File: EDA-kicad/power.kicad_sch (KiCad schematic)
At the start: 97 parts, among them SW1 EG25-switch-CSS-1210MC, SW2 MIC-switch-CSS-1210MC, SW3 CAM-switch-CSS-1210MC, U11 TPS65023BRSBR, U4 BQ25792RQMR, U6 BAT-CONNECTOR-FLTS22WR00, U7 22V-boost-AP3032KTR-G1, U8 MP3429GL-Z

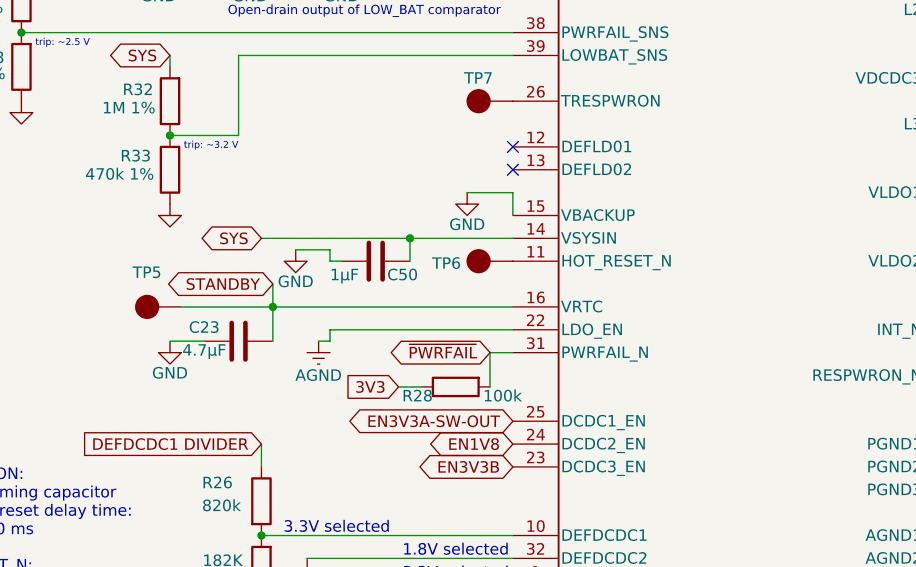
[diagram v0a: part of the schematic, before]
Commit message: applied no backup bat config to VSYSIN, removed standby label
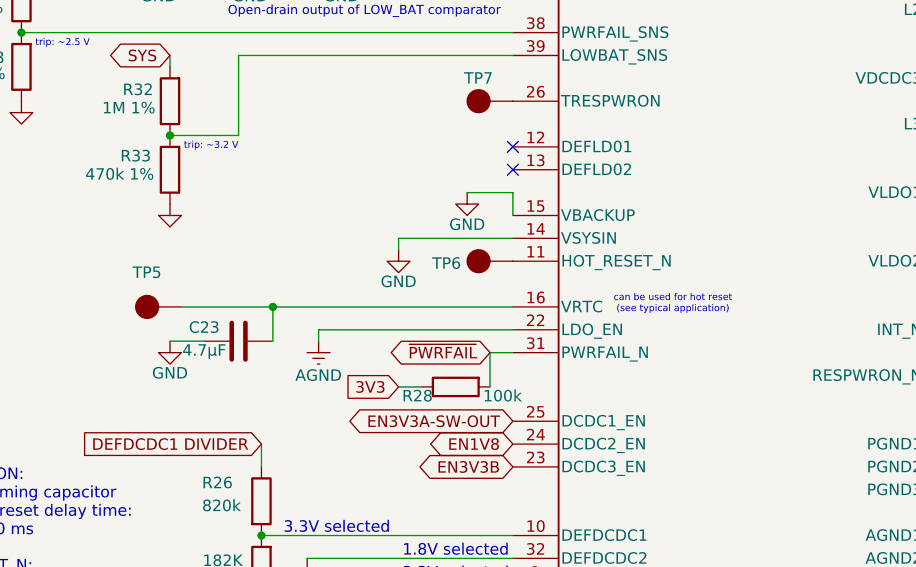
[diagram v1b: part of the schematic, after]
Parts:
- removed C50: 1μF, SPIRIT-footprints:0603-capacitor, symbol Device:C
- added C23: 4.7μF, SPIRIT-footprints:0603-capacitor, symbol Device:C
- added R33: 470k 1%, SPIRIT-footprints:0603-resistor, symbol Device:R
- renumbered C23 to C10, R33 to R8
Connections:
- net GND: now also U11.14 (VSYSIN), C23.1, R33.1; no longer C10.1
- net SYS: no longer U11.14 (VSYSIN)
- net at R32.1, U11.39 (LOWBAT_SNS): now also R33.2; no longer R8.2
- net STANDBY: no longer names the net of TP5.1 (A), U11.16 (VRTC)
- net STANDBY: now also C23.2; no longer C10.2
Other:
- note added: "can be used for hot reset (see typical application)"
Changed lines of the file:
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@@
 		)
 	)
+	(text "can be used for hot reset\n(see typical application)"
+		(exclude_from_sim no)
+		(at 321.31 135.636 0)
+		(effects
+			(font
+				(size 0.762 0.762)
+			)
+		)
+	)
 	(text "40mA selected for backlight LED"
 		(exclude_from_sim no)
@@
 	)
 	(junction
-		(at 292.1 128.27)
-		(diameter 0)
-		(color 0 0 0 0)
-	)
-	(junction
 		(at 146.05 238.76)
 		(diameter 0)
@@
 	(wire
 		(pts
-			(xy 283.21 130.81) (xy 284.48 130.81)
-		)
-		(stroke
-			(width 0)
-			(type default)
-		)
-	)
-	(wire
-		(pts
 			(xy 306.07 226.06) (xy 302.26 226.06)
 		)
@@
 	(wire
 		(pts
-			(xy 275.59 128.27) (xy 292.1 128.27)
-		)
-		(stroke
-			(width 0)
-			(type default)
-		)
-	)
-	(wire
-		(pts
 			(xy 298.45 81.28) (xy 298.45 88.9)
 		)
@@
 	(wire
 		(pts
-			(xy 283.21 138.43) (xy 303.53 138.43)
-		)
-		(stroke
-			(width 0)
-			(type default)
-		)
-	)
-	(wire
-		(pts
 			(xy 62.23 194.31) (xy 62.23 190.5)
 		)
@@
 	(wire
 		(pts
-			(xy 276.86 133.35) (xy 276.86 135.89)
-		)
-		(stroke
-			(width 0)
-			(type default)
-		)
-	)
-	(wire
-		(pts
 			(xy 369.57 119.38) (xy 372.11 119.38)
 		)
@@
 	(wire
 		(pts
-			(xy 372.11 93.98) (xy 369.57 93.98)
+			(xy 281.94 138.43) (xy 303.53 138.43)
 		)
 		(stroke
@@
 	(wire
 		(pts
-			(xy 298.45 81.28) (xy 299.72 80.01)
+			(xy 372.11 93.98) (xy 369.57 93.98)
 		)
 		(stroke
@@
 	(wire
 		(pts
-			(xy 212.09 179.07) (xy 209.55 179.07)
+			(xy 298.45 81.28) (xy 299.72 80.01)
 		)
 		(stroke
@@
 	(wire
 		(pts
-			(xy 142.24 82.55) (xy 140.97 82.55)
+			(xy 212.09 179.07) (xy 209.55 179.07)
 		)
 		(stroke
@@
 	(wire
 		(pts
-			(xy 93.98 246.38) (xy 110.49 246.38)
+			(xy 142.24 82.55) (xy 140.97 82.55)
 		)
 		(stroke
@@
 	(wire
 		(pts
-			(xy 157.48 81.28) (xy 157.48 82.55)
+			(xy 93.98 246.38) (xy 110.49 246.38)
 		)
 		(stroke
@@
 	(wire
 		(pts
-			(xy 135.89 58.42) (xy 133.35 58.42)
+			(xy 157.48 81.28) (xy 157.48 82.55)
 		)
 		(stroke
@@
 	(wire
 		(pts
-			(xy 279.4 129.54) (xy 283.21 129.54)
+			(xy 135.89 58.42) (xy 133.35 58.42)
 		)
 		(stroke
@@
 	(wire
 		(pts
-			(xy 292.1 128.27) (xy 292.1 130.81)
-		)
-		(stroke
-			(width 0)
-			(type default)
-		)
-	)
-	(wire
-		(pts
 			(xy 248.92 96.52) (xy 248.92 97.79)
 		)
@@
 	(wire
 		(pts
-			(xy 283.21 139.7) (xy 283.21 138.43)
-		)
-		(stroke
-			(width 0)
-			(type default)
-		)
-	)
-	(wire
-		(pts
 			(xy 130.81 74.93) (xy 130.81 77.47)
 		)
@@
 	(wire
 		(pts
-			(xy 283.21 129.54) (xy 283.21 130.81)
-		)
-		(stroke
-			(width 0)
-			(type default)
-		)
-	)
-	(wire
-		(pts
 			(xy 369.57 106.68) (xy 372.11 106.68)
 		)
@@
 	(wire
 		(pts
-			(xy 281.94 139.7) (xy 283.21 139.7)
+			(xy 290.83 128.27) (xy 290.83 129.54)
 		)
 		(stroke
@@
 	(wire
 		(pts
-			(xy 78.74 118.11) (xy 83.82 118.11)
+			(xy 281.94 138.43) (xy 281.94 139.7)
 		)
 		(stroke
@@
 	(wire
 		(pts
-			(xy 275.59 151.13) (xy 275.59 153.67)
+			(xy 78.74 118.11) (xy 83.82 118.11)
 		)
 		(stroke
@@
 	(wire
 		(pts
-			(xy 93.98 250.19) (xy 99.06 250.19)
+			(xy 275.59 151.13) (xy 275.59 153.67)
 		)
 		(stroke
@@
 	(wire
 		(pts
-			(xy 148.59 106.68) (xy 148.59 107.95)
+			(xy 93.98 250.19) (xy 99.06 250.19)
 		)
 		(stroke
@@
 	(wire
 		(pts
-			(xy 292.1 128.27) (xy 303.53 128.27)
+			(xy 148.59 106.68) (xy 148.59 107.95)
 		)
 		(stroke
@@
 	(wire
 		(pts
+			(xy 290.83 128.27) (xy 303.53 128.27)
+		)
+		(stroke
+			(width 0)
+			(type default)
+		)
+	)
+	(wire
+		(pts
 			(xy 379.73 110.49) (xy 384.81 110.49)
 		)
@@
 		)
 	)
-	(global_label "SYS"
-		(shape bidirectional)
-		(at 275.59 128.27 180)
-		(fields_autoplaced yes)
-		(effects
-			(font
-				(size 1.27 1.27)
-			)
-			(justify right)
-		)
-		(property "Intersheetrefs" "${INTERSHEET_REFS}"
-			(at 267.9859 128.27 0)
-			(effects
-				(font
-					(size 1.27 1.27)
-				)
-				(justify right)
-				(hide yes)
-			)
-		)
-	)
 	(global_label "~{PWRFAIL}"
 		(shape bidirectional)
@@
 		)
 	)
-	(global_label "STANDBY"
-		(shape bidirectional)
-		(at 276.86 133.35 180)
-		(fields_autoplaced yes)
-		(effects
-			(font
-				(size 1.27 1.27)
-			)
-			(justify right)
-		)
-		(property "Intersheetrefs" "${INTERSHEET_REFS}"
-			(at 269.2559 133.35 0)
-			(effects
-				(font
-					(size 1.27 1.27)
-				)
-				(justify right)
-				(hide yes)
-			)
-		)
-	)
 	(global_label "REGN"
 		(shape bidirectional)
@@
 	(symbol
 		(lib_id "Device:C")
-		(at 288.29 130.81 270)
-		(unit 1)
-		(exclude_from_sim no)
-		(in_bom yes)
-		(on_board yes)
-		(dnp no)
-		(property "Reference" "C50"
-			(at 289.56 132.334 90)
-			(effects
-				(font
-					(size 1.27 1.27)
-				)
-				(justify left)
-			)
-		)
-		(property "Value" "1μF"
-			(at 283.21 132.334 90)
-			(effects
-				(font
-					(size 1.27 1.27)
-				)
-				(justify left)
-			)
-		)
-		(property "Footprint" "SPIRIT-footprints:0603-capacitor"
-			(at 284.48 131.7752 0)
-			(effects
-				(font
-					(size 1.27 1.27)
-				)
-				(hide yes)
-			)
-		)
-		(property "Datasheet" "~"
-			(at 288.29 130.81 0)
-			(effects
-				(font
-					(size 1.27 1.27)
-				)
-				(hide yes)
-			)
-		)
-		(property "Description" "Unpolarized capacitor"
-			(at 288.29 130.81 0)
-			(effects
-				(font
-					(size 1.27 1.27)
-				)
-				(hide yes)
-			)
-		)
-		(property "MPN" "CC0603KRX5R8BB105"
-			(at 288.29 130.81 0)
-			(effects
-				(font
-					(size 1.27 1.27)
-				)
-				(hide yes)
-			)
-		)
-		(pin "2"
-		)
-		(pin "1"
-		)
-		(instances
-			(project "cm5-carrier"
-				(path "/28c5e4fe-1ec7-4477-97f0-d2ec1401fad5/59851108-1ec5-49a1-aa9b-d5428f895885"
-					(reference "C50")
-					(unit 1)
-				)
-			)
-			(project "power"
-				(path "/446f2954-4486-4a73-ab5d-988e1515679d"
-					(reference "C?")
-					(unit 1)
-				)
-			)
-		)
-	)
-	(symbol
-		(lib_id "Device:C")
 		(at 137.16 243.84 0)
 		(unit 1)
@@
 		(lib_name "GND_11")
 		(lib_id "power:GND")
-		(at 279.4 129.54 0)
+		(at 290.83 129.54 0)
 		(unit 1)
 		(exclude_from_sim no)
@@
 		(dnp no)
 		(property "Reference" "#PWR0147"
-			(at 279.4 135.89 0)
+			(at 290.83 135.89 0)
 			(effects
 				(font
@@
 		)
 		(property "Value" "GND"
-			(at 279.4 133.096 0)
+			(at 290.83 133.096 0)
 			(effects
 				(font
@@
 		)
 		(property "Footprint" ""
-			(at 279.4 129.54 0)
+			(at 290.83 129.54 0)
 			(effects
 				(font
@@
 		)
 		(property "Datasheet" ""
-			(at 279.4 129.54 0)
+			(at 290.83 129.54 0)
 			(effects
 				(font
@@
 		)
 		(property "Description" "Power symbol creates a global label with name \"GND\" , ground"
-			(at 279.4 129.54 0)
+			(at 290.83 129.54 0)
 			(effects
 				(font

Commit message: add testpad to INT
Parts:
- added TP8: test-pad-1, SPIRIT-footprints:test-pad-1, symbol SPIRIT-components:test-pad-1
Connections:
- net ~{TPS INT}: now also TP8.1 (A)
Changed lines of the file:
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@@
 	)
 	(junction
+		(at 360.68 138.43)
+		(diameter 0)
+		(color 0 0 0 0)
+	)
+	(junction
 		(at 167.64 95.25)
 		(diameter 0)
@@
 	(wire
 		(pts
-			(xy 372.11 92.71) (xy 372.11 93.98)
-		)
-		(stroke
-			(width 0)
-			(type default)
-		)
-	)
-	(wire
-		(pts
 			(xy 133.35 67.31) (xy 135.89 67.31)
 		)
@@
 	(wire
 		(pts
-			(xy 372.11 118.11) (xy 372.11 119.38)
-		)
-		(stroke
-			(width 0)
-			(type default)
-		)
-	)
-	(wire
-		(pts
 			(xy 62.23 187.96) (xy 63.5 187.96)
 		)
@@
 	(wire
 		(pts
-			(xy 372.11 105.41) (xy 372.11 106.68)
-		)
-		(stroke
-			(width 0)
-			(type default)
-		)
-	)
-	(wire
-		(pts
 			(xy 290.83 166.37) (xy 303.53 166.37)
 		)
@@
 	(wire
 		(pts
-			(xy 369.57 119.38) (xy 372.11 119.38)
+			(xy 369.57 119.38) (xy 373.38 119.38)
 		)
 		(stroke
@@
 	(wire
 		(pts
-			(xy 372.11 93.98) (xy 369.57 93.98)
+			(xy 369.57 93.98) (xy 373.38 93.98)
 		)
 		(stroke
@@
 	(wire
 		(pts
-			(xy 354.33 138.43) (xy 363.22 138.43)
+			(xy 354.33 138.43) (xy 360.68 138.43)
 		)
 		(stroke
@@
 	(wire
 		(pts
-			(xy 372.11 105.41) (xy 374.65 105.41)
-		)
-		(stroke
-			(width 0)
-			(type default)
-		)
-	)
-	(wire
-		(pts
 			(xy 135.89 125.73) (xy 130.81 125.73)
 		)
@@
 	(wire
 		(pts
-			(xy 369.57 106.68) (xy 372.11 106.68)
+			(xy 369.57 106.68) (xy 373.38 106.68)
 		)
 		(stroke
@@
 	(wire
 		(pts
-			(xy 374.65 92.71) (xy 372.11 92.71)
-		)
-		(stroke
-			(width 0)
-			(type default)
-		)
-	)
-	(wire
-		(pts
 			(xy 157.48 83.82) (xy 157.48 82.55)
 		)
@@
 	(wire
 		(pts
-			(xy 372.11 118.11) (xy 374.65 118.11)
+			(xy 243.84 74.93) (xy 245.11 74.93)
 		)
 		(stroke
@@
 	(wire
 		(pts
-			(xy 243.84 74.93) (xy 245.11 74.93)
+			(xy 290.83 128.27) (xy 303.53 128.27)
 		)
 		(stroke
@@
 	(wire
 		(pts
-			(xy 290.83 128.27) (xy 303.53 128.27)
+			(xy 379.73 110.49) (xy 384.81 110.49)
 		)
 		(stroke
@@
 	(wire
 		(pts
-			(xy 379.73 110.49) (xy 384.81 110.49)
+			(xy 69.85 72.39) (xy 69.85 73.66)
 		)
 		(stroke
@@
 	(wire
 		(pts
-			(xy 69.85 72.39) (xy 69.85 73.66)
+			(xy 273.05 86.36) (xy 274.32 85.09)
 		)
 		(stroke
@@
 	(wire
 		(pts
-			(xy 273.05 86.36) (xy 274.32 85.09)
+			(xy 360.68 138.43) (xy 363.22 138.43)
 		)
 		(stroke
@@
 		(lib_name "GND_11")
 		(lib_id "power:GND")
-		(at 374.65 92.71 0)
+		(at 373.38 93.98 0)
 		(unit 1)
 		(exclude_from_sim no)
@@
 		(dnp no)
 		(property "Reference" "#PWR0151"
-			(at 374.65 99.06 0)
+			(at 373.38 100.33 0)
 			(effects
 				(font
@@
 		)
 		(property "Value" "GND"
-			(at 374.65 96.266 0)
+			(at 373.38 97.536 0)
 			(effects
 				(font
 					(size 1.27 1.27)
 				)
+				(hide yes)
 			)
 		)
 		(property "Footprint" ""
-			(at 374.65 92.71 0)
+			(at 373.38 93.98 0)
 			(effects
 				(font
@@
 		)
 		(property "Datasheet" ""
-			(at 374.65 92.71 0)
+			(at 373.38 93.98 0)
 			(effects
 				(font
@@
 		)
 		(property "Description" "Power symbol creates a global label with name \"GND\" , ground"
-			(at 374.65 92.71 0)
+			(at 373.38 93.98 0)
 			(effects
 				(font
@@
 	)
 	(symbol
+		(lib_id "SPIRIT-components:test-pad-1")
+		(at 361.95 142.24 270)
+		(unit 1)
+		(exclude_from_sim no)
+		(in_bom yes)
+		(on_board yes)
+		(dnp no)
+		(property "Reference" "TP8"
+			(at 360.934 145.796 90)
+			(effects
+				(font
+					(size 1.27 1.27)
+				)
+			)
+		)
+		(property "Value" "test-pad-1"
+			(at 365.76 142.24 0)
+			(effects
+				(font
+					(size 1.27 1.27)
+				)
+				(hide yes)
+			)
+		)
+		(property "Footprint" "SPIRIT-footprints:test-pad-1"
+			(at 361.95 142.24 0)
+			(effects
+				(font
+					(size 1.27 1.27)
+				)
+				(hide yes)
+			)
+		)
+		(property "Datasheet" ""
+			(at 361.95 142.24 0)
+			(effects
+				(font
+					(size 1.27 1.27)
+				)
+				(hide yes)
+			)
+		)
+		(property "Description" ""
+			(at 361.95 142.24 0)
+			(effects
+				(font
+					(size 1.27 1.27)
+				)
+				(hide yes)
+			)
+		)
+		(pin "1"
+		)
+		(instances
+			(project "cm5-carrier"
+				(path "/28c5e4fe-1ec7-4477-97f0-d2ec1401fad5/59851108-1ec5-49a1-aa9b-d5428f895885"
+					(reference "TP8")
+					(unit 1)
+				)
+			)
+		)
+	)
+	(symbol
 		(lib_id "Device:C")
 		(at 161.29 99.06 0)
@@
 					(size 1.27 1.27)
 				)
+				(hide yes)
 			)
 		)
@@
 		(lib_name "GND_11")
 		(lib_id "power:GND")
-		(at 374.65 118.11 0)
+		(at 373.38 119.38 0)
 		(unit 1)
 		(exclude_from_sim no)
@@
 		(dnp no)
 		(property "Reference" "#PWR0149"
-			(at 374.65 124.46 0)
+			(at 373.38 125.73 0)
 			(effects
 				(font
@@
 		)
 		(property "Value" "GND"
-			(at 374.65 121.666 0)
+			(at 373.38 122.936 0)
 			(effects
 				(font
 					(size 1.27 1.27)
 				)
+				(hide yes)
 			)
 		)
 		(property "Footprint" ""
-			(at 374.65 118.11 0)
+			(at 373.38 119.38 0)
 			(effects
 				(font
@@
 		)
 		(property "Datasheet" ""
-			(at 374.65 118.11 0)
+			(at 373.38 119.38 0)
 			(effects
 				(font
@@
 		)
 		(property "Description" "Power symbol creates a global label with name \"GND\" , ground"
-			(at 374.65 118.11 0)
+			(at 373.38 119.38 0)
 			(effects
 				(font
@@
 					(size 1.27 1.27)
 				)
+				(hide yes)
 			)
 		)
@@
 		(lib_name "GND_11")
 		(lib_id "power:GND")
-		(at 374.65 105.41 0)
+		(at 373.38 106.68 0)
 		(unit 1)
 		(exclude_from_sim no)
@@
 		(dnp no)
 		(property "Reference" "#PWR0150"
-			(at 374.65 111.76 0)
+			(at 373.38 113.03 0)
 			(effects
 				(font
@@
 		)
 		(property "Value" "GND"
-			(at 374.65 108.966 0)
+			(at 373.38 110.236 0)
 			(effects
 				(font
 					(size 1.27 1.27)
 				)
+				(hide yes)
 			)
 		)
 		(property "Footprint" ""
-			(at 374.65 105.41 0)
+			(at 373.38 106.68 0)
 			(effects
 				(font
@@
 		)
 		(property "Datasheet" ""
-			(at 374.65 105.41 0)
+			(at 373.38 106.68 0)
 			(effects
 				(font
@@
 		)
 		(property "Description" "Power symbol creates a global label with name \"GND\" , ground"
-			(at 374.65 105.41 0)
+			(at 373.38 106.68 0)
 			(effects
 				(font
@@
 					(size 1.27 1.27)
 				)
+				(hide yes)
 			)
 		)
@@
 					(size 1.27 1.27)
 				)
+				(hide yes)
 			)
 		)
